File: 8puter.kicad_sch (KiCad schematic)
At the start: 32 parts, among them J1 PWR-DC, U1 74HC00, X1 ECS-2200BX-100

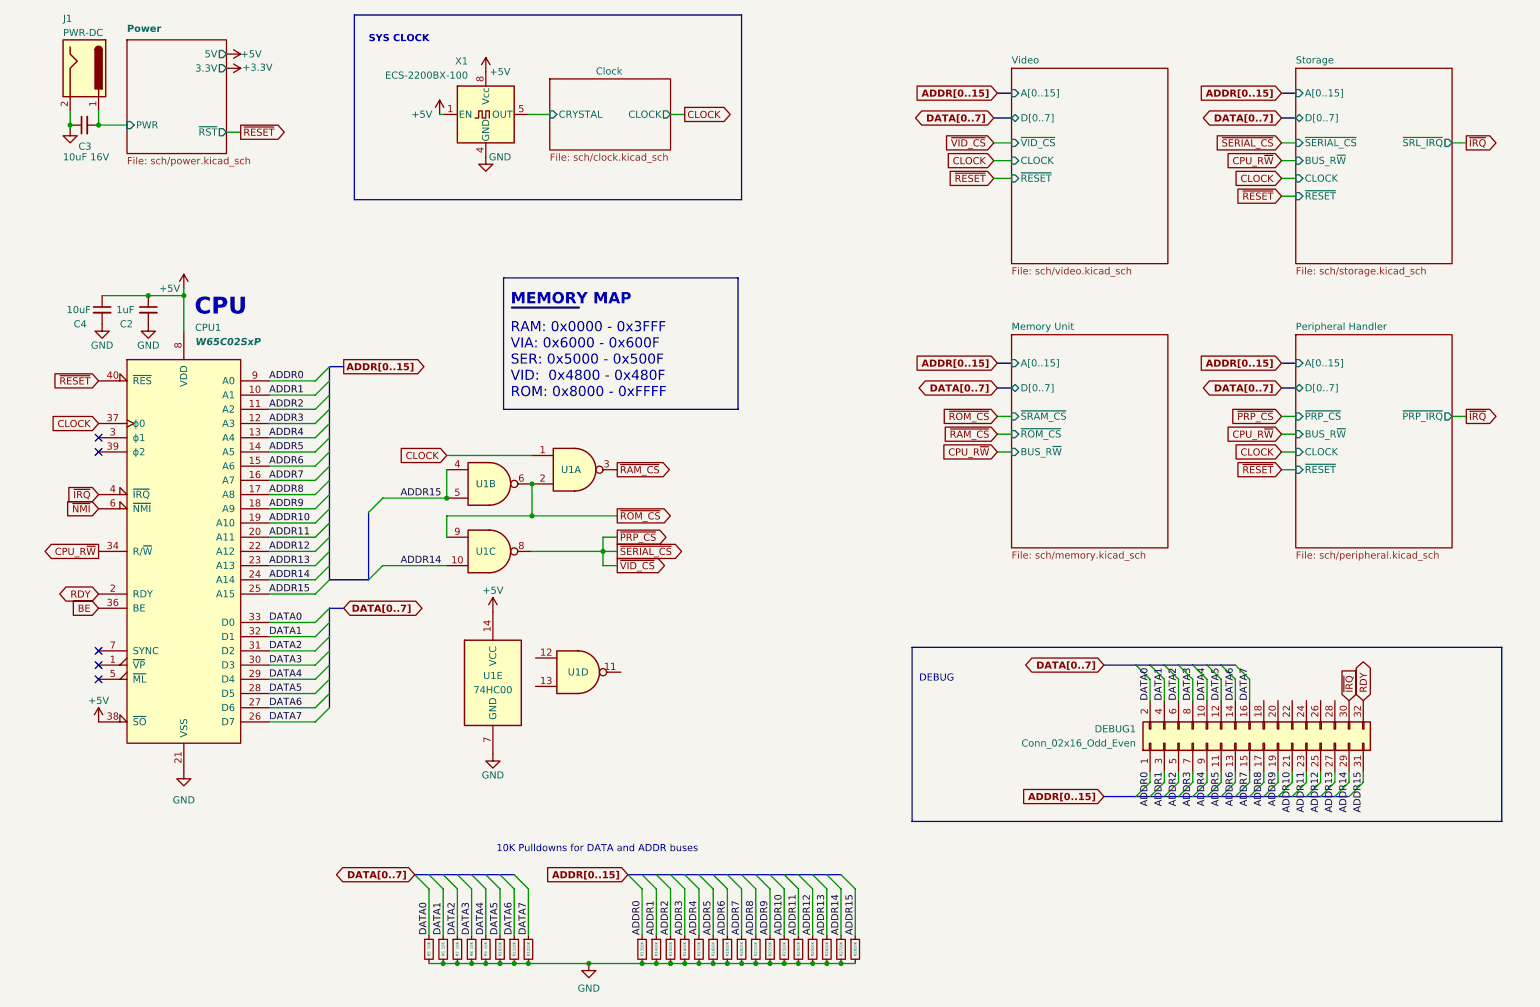
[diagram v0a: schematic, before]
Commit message: fix peripherals, add SPI
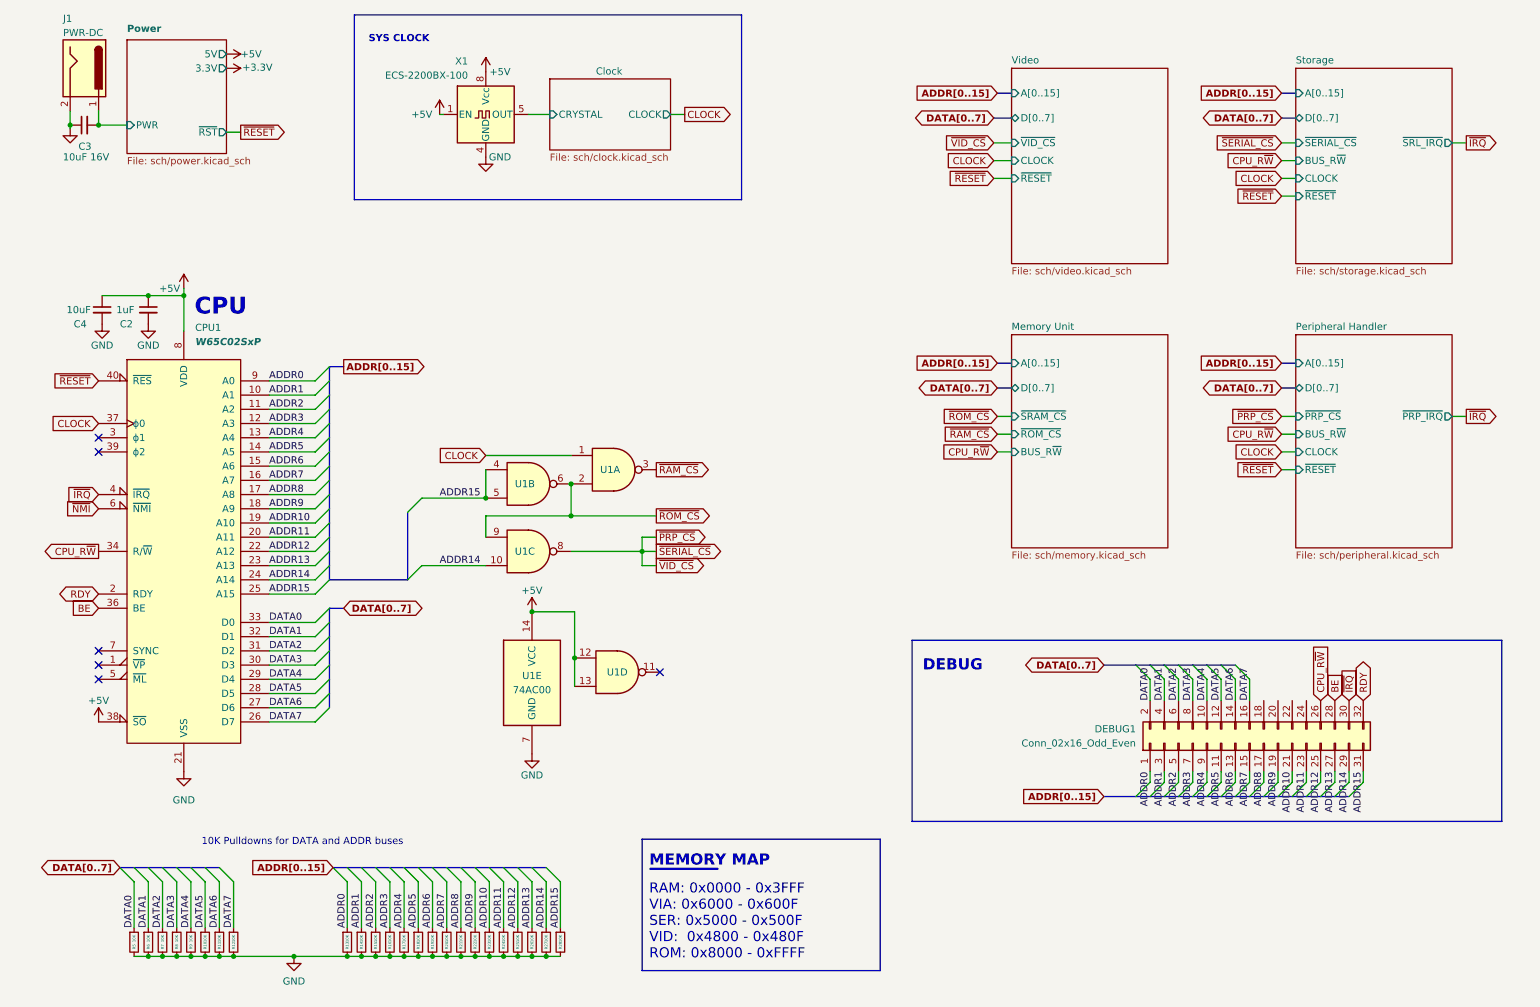
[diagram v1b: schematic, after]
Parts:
- U1: value 74HC00 -> 74AC00; footprint (none) -> Package_SO:TSSOP-14_4.4x5mm_P0.65mm
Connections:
- net +5V: now also U1.12, U1.13
- net BE: now also DEBUG1.28 (Pin_28)
- net CPU_R~{W}: now also DEBUG1.26 (Pin_26)
- no-connect marks 5 -> 6
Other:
- moved on the sheet: R10, R11, R12, R13, R14, R15, R16, R17, R18, R19, R20, R21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

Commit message: Cleanup board
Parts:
- C3: symbol Device:C_Small -> Device:C_Polarized_Small
- R10, R11, R12, R13, R14, R15, R16, R17, R18, R19, R20, R21, R22, R23, R24, R25, R26, R27, R28, R5, R6, R7, R8, R9: value 10K -> (none)
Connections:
- net GND: now also C3.2; no longer C3.1
- net Power/PWR: now also C3.1; no longer C3.2
- net ~{NMI}: no longer names the net of CPU1.6 (~{NMI})
- no-connect marks 6 -> 11

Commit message: Clearances
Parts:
- R10, R11, R12, R13, R14, R15, R16, R17, R18, R19, R20, R21, R22, R23, R24, R25, R26, R27, R28, R5, R6, R7, R8, R9: value (none) -> 1K
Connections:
- net +5V: now also DEBUG1.20 (Pin_20)
- net CLOCK: now also DEBUG1.24 (Pin_24)
- net GND: now also DEBUG1.18 (Pin_18)
- no-connect marks 11 -> 8

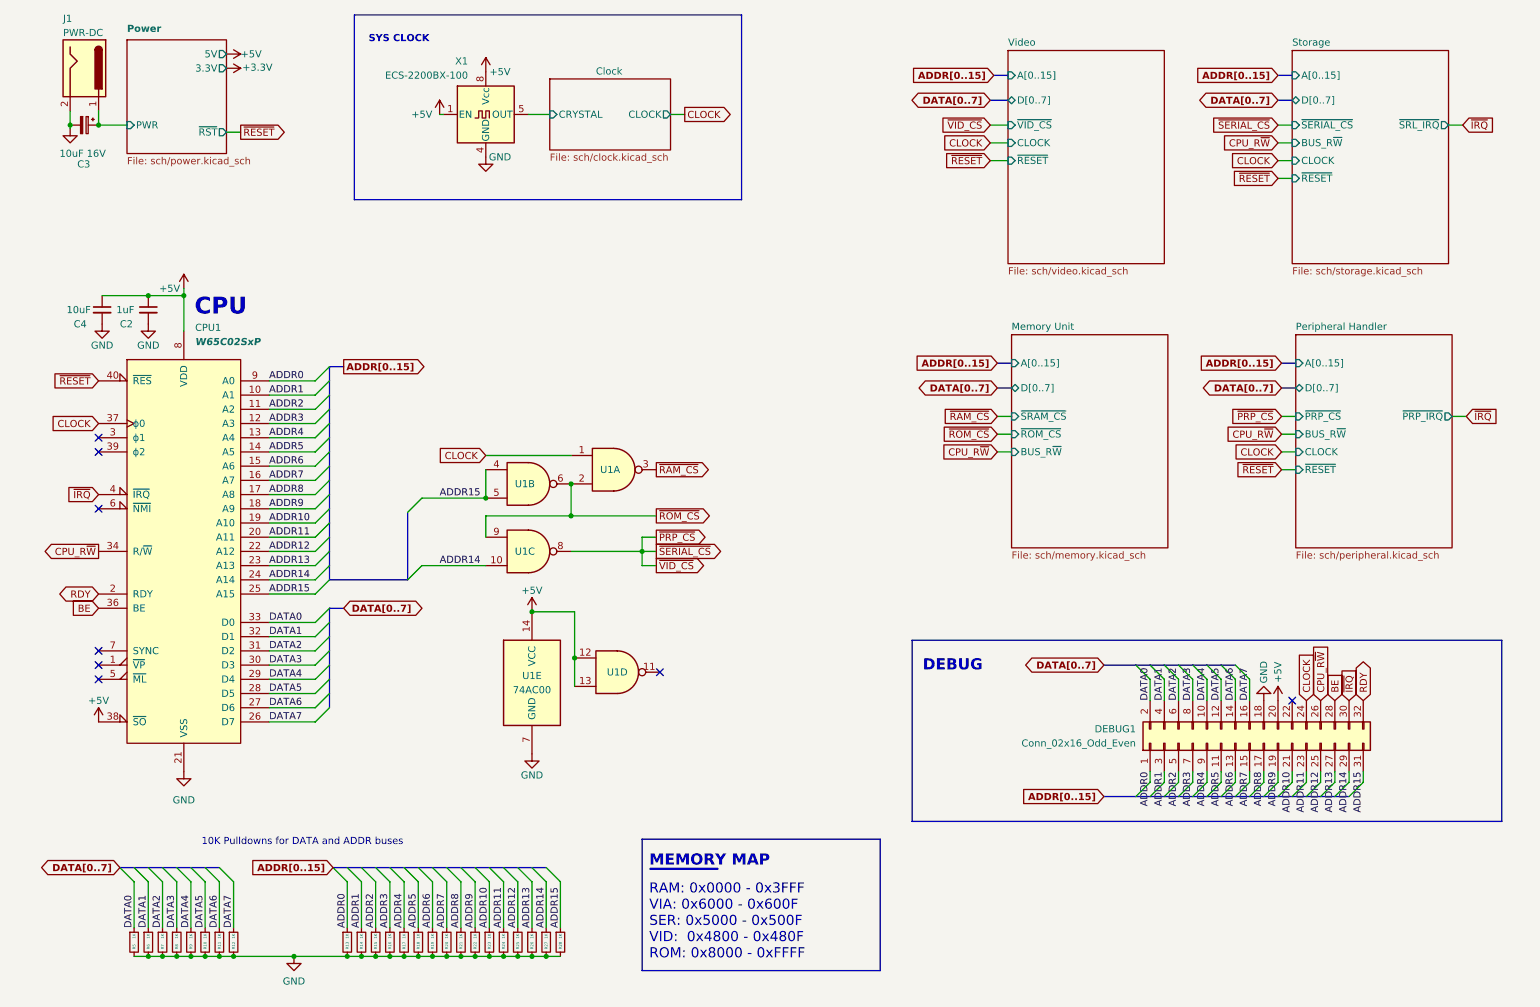
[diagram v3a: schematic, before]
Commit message: Huge mistake CPU fp
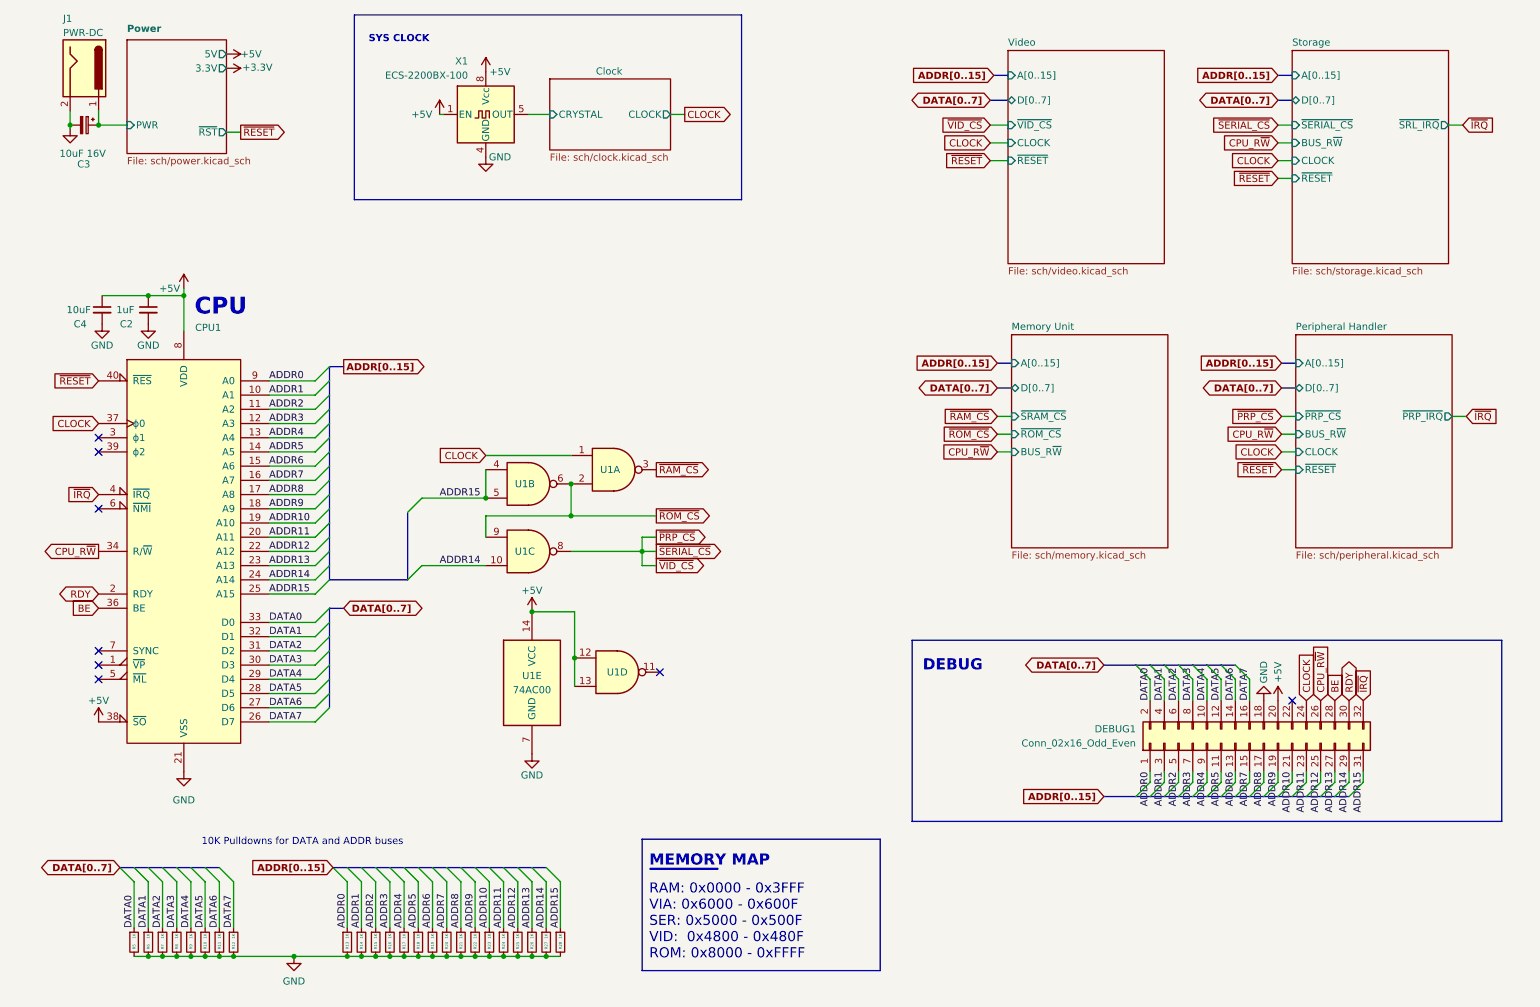
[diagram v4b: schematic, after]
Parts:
- CPU1: value W65C02SxP -> (none); footprint Package_DIP:DIP-40_W25.4mm_LongPads -> (none)
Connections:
- net RDY: now also DEBUG1.30 (Pin_30); no longer DEBUG1.32 (Pin_32)
- net ~{IRQ}: now also DEBUG1.32 (Pin_32); no longer DEBUG1.30 (Pin_30)
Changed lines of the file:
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@@
     )
   )
-  (global_label "RDY" (shape bidirectional) (at 257.81 141.605 90) (fields_autoplaced)
+  (global_label "RDY" (shape bidirectional) (at 255.27 141.605 90) (fields_autoplaced)
     (effects (font (size 1.27 1.27)) (justify left))
-    (property "Intersheet References" "${INTERSHEET_REFS}" (id 0) (at 257.8894 135.5633 90)
+    (property "Intersheet References" "${INTERSHEET_REFS}" (id 0) (at 255.3494 135.5633 90)
       (effects (font (size 1.27 1.27)) (justify left) hide)
     )
@@
     )
   )
-  (global_label "~{IRQ}" (shape input) (at 255.27 141.605 90) (fields_autoplaced)
+  (global_label "~{IRQ}" (shape input) (at 257.81 141.605 90) (fields_autoplaced)
     (effects (font (size 1.27 1.27)) (justify left))
-    (property "Intersheet References" "${INTERSHEET_REFS}" (id 0) (at 255.1906 135.9867 90)
+    (property "Intersheet References" "${INTERSHEET_REFS}" (id 0) (at 257.7306 135.9867 90)
       (effects (font (size 1.27 1.27)) (justify left) hide)
     )
@@
       (effects (font (size 1.27 1.27)) (justify left))
     )
-    (property "Value" "W65C02SxP" (id 1) (at 49.0094 77.47 0)
+    (property "Value" "" (id 1) (at 49.0094 77.47 0)
       (effects (font (size 1.27 1.27) bold italic) (justify left))
     )
-    (property "Footprint" "Package_DIP:DIP-40_W25.4mm_LongPads" (id 2) (at 46.99 64.135 0)
+    (property "Footprint" "" (id 2) (at 46.99 64.135 0)
       (effects (font (size 1.27 1.27)) hide)
     )
@@
     )
     (path "/4097d8ff-d5fe-4916-b054-086b1f2834f9"
-      (reference "CPU1") (unit 1) (value "W65C02SxP") (footprint "Package_DIP:DIP-40_W25.4mm_LongPads")
+      (reference "CPU1") (unit 1) (value "W65C02SxP") (footprint "Package_DIP:DIP-40_W15.24mm_LongPads")
     )
     (path "/59d6507d-8c01-4b37-beee-b798f6eef3f6/07a43ecd-1101-44b6-a223-07a702d03c42"

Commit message: bigger header pins
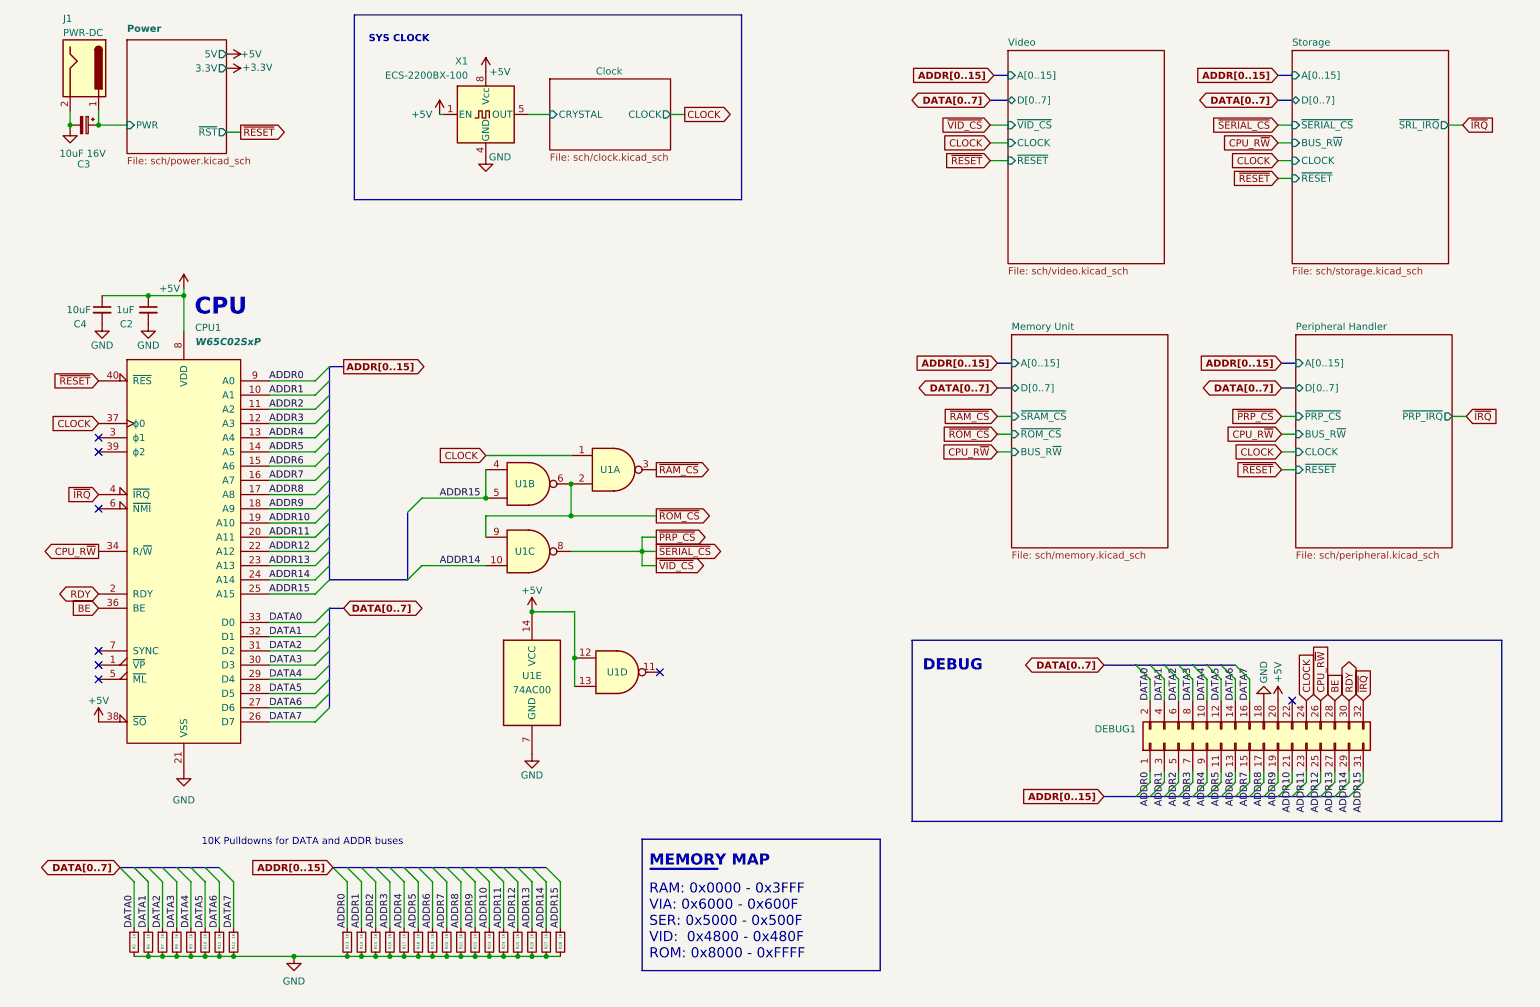
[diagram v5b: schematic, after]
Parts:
- CPU1: value (none) -> W65C02SxP; footprint (none) -> Package_DIP:DIP-40_W15.24mm_LongPads
- DEBUG1: value Conn_02x16_Odd_Even -> (none); footprint Connector_PinHeader_2.00mm:PinHeader_2x16_P2.00mm_Vertical -> (none)
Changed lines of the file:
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@@
       (effects (font (size 1.27 1.27)) (justify left))
     )
-    (property "Value" "Conn_02x16_Odd_Even" (id 1) (at 217.17 149.2249 90)
-      (effects (font (size 1.27 1.27)) (justify left))
-    )
-    (property "Footprint" "Connector_PinHeader_2.00mm:PinHeader_2x16_P2.00mm_Vertical" (id 2) (at 237.49 149.225 0)
+    (property "Value" "" (id 1) (at 217.17 149.2249 90)
+      (effects (font (size 1.27 1.27)) (justify left))
+    )
+    (property "Footprint" "" (id 2) (at 237.49 149.225 0)
       (effects (font (size 1.27 1.27)) hide)
     )
@@
       (effects (font (size 1.27 1.27)) (justify left))
     )
-    (property "Value" "" (id 1) (at 49.0094 77.47 0)
+    (property "Value" "W65C02SxP" (id 1) (at 49.0094 77.47 0)
       (effects (font (size 1.27 1.27) bold italic) (justify left))
     )
-    (property "Footprint" "" (id 2) (at 46.99 64.135 0)
+    (property "Footprint" "Package_DIP:DIP-40_W15.24mm_LongPads" (id 2) (at 46.99 64.135 0)
       (effects (font (size 1.27 1.27)) hide)
     )
@@
     )
     (path "/59d6507d-8c01-4b37-beee-b798f6eef3f6/07a43ecd-1101-44b6-a223-07a702d03c42"
-      (reference "CS_SEL1") (unit 1) (value "Conn_02x03_Odd_Even") (footprint "Connector_PinHeader_2.00mm:PinHeader_2x03_P2.00mm_Vertical")
+      (reference "CS_SEL1") (unit 1) (value "Conn_02x03_Odd_Even") (footprint "Connector_PinHeader_2.54mm:PinHeader_2x03_P2.54mm_Vertical")
     )
     (path "/1cf5bdd1-35d3-4238-800b-96633c0c913b/7b92496e-8832-462c-9134-c9933855ed1d"
@@
     )
     (path "/30a6b211-0dc3-4f51-bcb7-52fe848ee97e"
-      (reference "DEBUG1") (unit 1) (value "Conn_02x16_Odd_Even") (footprint "Connector_PinHeader_2.00mm:PinHeader_2x16_P2.00mm_Vertical")
+      (reference "DEBUG1") (unit 1) (value "Conn_02x16_Odd_Even") (footprint "Connector_PinHeader_2.54mm:PinHeader_2x16_P2.54mm_Vertical")
     )
     (path "/a54297d9-3f68-4e1b-8e71-284b03256929"
@@
     )
     (path "/287b8d7b-7977-45e3-a8a2-fb0a63aeaa82/29f5a9a2-94a6-4cdc-a8e7-84648a7a8222"
-      (reference "PERIPHERAL1") (unit 1) (value "Conn_02x08_Odd_Even") (footprint "Connector_PinHeader_2.00mm:PinHeader_2x08_P2.00mm_Vertical")
+      (reference "PERP1") (unit 1) (value "Conn_02x08_Odd_Even") (footprint "Connector_PinHeader_2.54mm:PinHeader_2x08_P2.54mm_Vertical")
     )
     (path "/afee8228-6c57-4fb7-9c62-64e9ad6d349f/971f36f6-d845-4710-b9e9-e890521ffeb6"
-      (reference "PROG1") (unit 1) (value "Conn_01x05") (footprint "Connector_PinHeader_2.00mm:PinHeader_1x05_P2.00mm_Vertical")
+      (reference "PROG1") (unit 1) (value "Conn_01x05") (footprint "Connector_PinHeader_2.54mm:PinHeader_1x05_P2.54mm_Vertical")
     )
     (path "/287b8d7b-7977-45e3-a8a2-fb0a63aeaa82/d9899845-bf60-4c8f-bb0b-a0ea4cb0fe86"
@@
     )
     (path "/6fb476cc-0d35-4ef8-90a2-1a1fd6ffea47/5d9b78bb-748c-4a68-a8c0-abb1a6517e13"
-      (reference "ROM_WRITE1") (unit 1) (value "Conn_01x03") (footprint "Connector_PinHeader_2.00mm:PinHeader_1x03_P2.00mm_Vertical")
+      (reference "ROM_WRITE1") (unit 1) (value "Conn_01x03") (footprint "Connector_PinHeader_2.54mm:PinHeader_1x03_P2.54mm_Vertical")
     )
     (path "/8c24dcfd-eb2d-4d97-9da8-040e7b195117/9f06bc3d-ce21-4b96-bdb4-845d24d9c3ea"
@@
     )
     (path "/8c24dcfd-eb2d-4d97-9da8-040e7b195117/9d21f321-3993-42a6-aedd-e9bd5deba8c3"
-      (reference "SPI1") (unit 1) (value "Conn_01x06") (footprint "Connector_PinHeader_2.00mm:PinHeader_1x06_P2.00mm_Vertical")
+      (reference "SPI1") (unit 1) (value "Conn_01x06") (footprint "Connector_PinHeader_2.54mm:PinHeader_1x06_P2.54mm_Vertical")
     )
     (path "/59d6507d-8c01-4b37-beee-b798f6eef3f6/9759b995-89b1-4406-bbbe-2b1fe1a42713"
